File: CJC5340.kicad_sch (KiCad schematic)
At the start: 14 parts

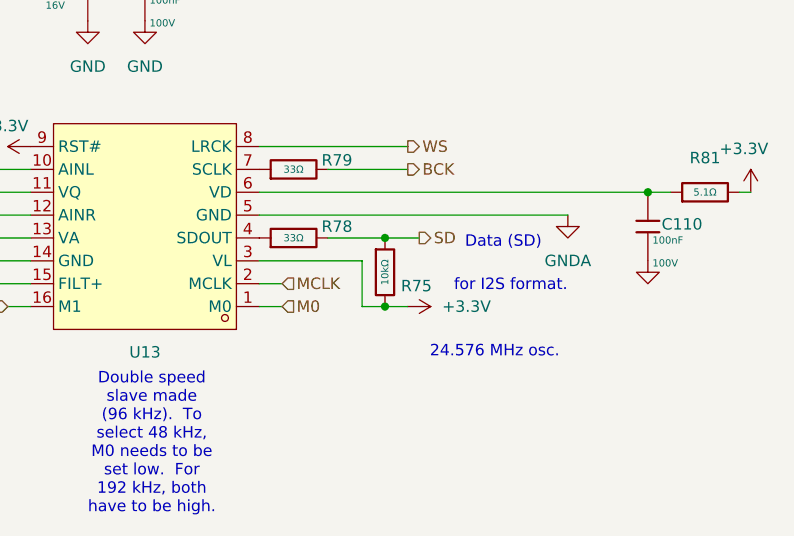
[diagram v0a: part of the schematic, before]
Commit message: Placed the second ADC
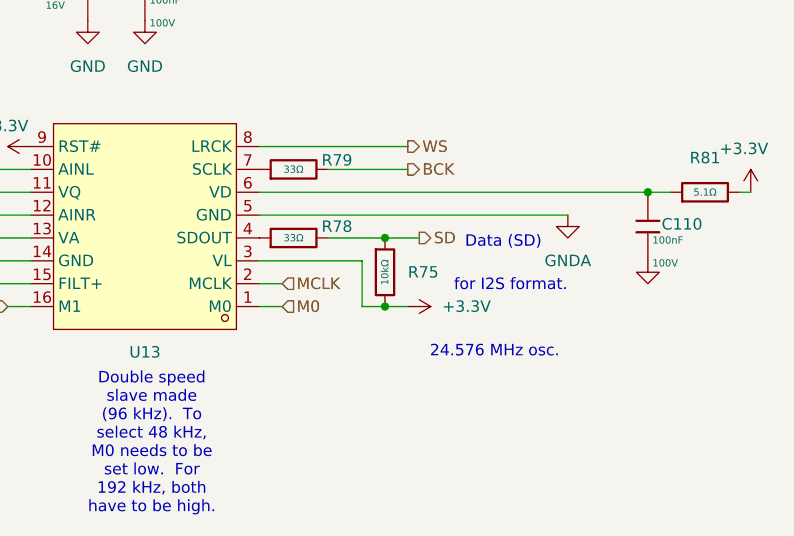
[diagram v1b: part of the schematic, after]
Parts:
- removed R75: 10kΩ, PCM_JLCPCB:R_0402, symbol PCM_JLCPCB-Resistors:0402,10kΩ
- added R75: 10kΩ, PCM_JLCPCB:R_0805, symbol PCM_JLCPCB-Resistors:0805,10kΩ
- C104, C108, C113, C99: Manufacturer AVX -> (none)
- C106, C109, C110, C112, C114: Manufacturer Samsung Electro-Mechanics -> (none)
- R78, R79, R81: Manufacturer UNI-ROYAL(Uniroyal Elec) -> (none)
- U13: Manufacturer ESHINE(光华芯) -> (none)
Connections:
- net +3.3V: now also R75.2
- net SD: now also R75.1

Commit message: More routing
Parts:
- R75: Manufacturer UNI-ROYAL(Uniroyal Elec) -> (none)
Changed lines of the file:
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@@
-			)
-		)
-		(property "Manufacturer" "UNI-ROYAL(Uniroyal Elec)"
-			(at 218.44 93.98 0)
-			(hide yes)
-			(show_name no)
-			(do_not_autoplace no)
-			(effects
-				(font
-					(size 1.27 1.27)
-				)
 			)
 		)

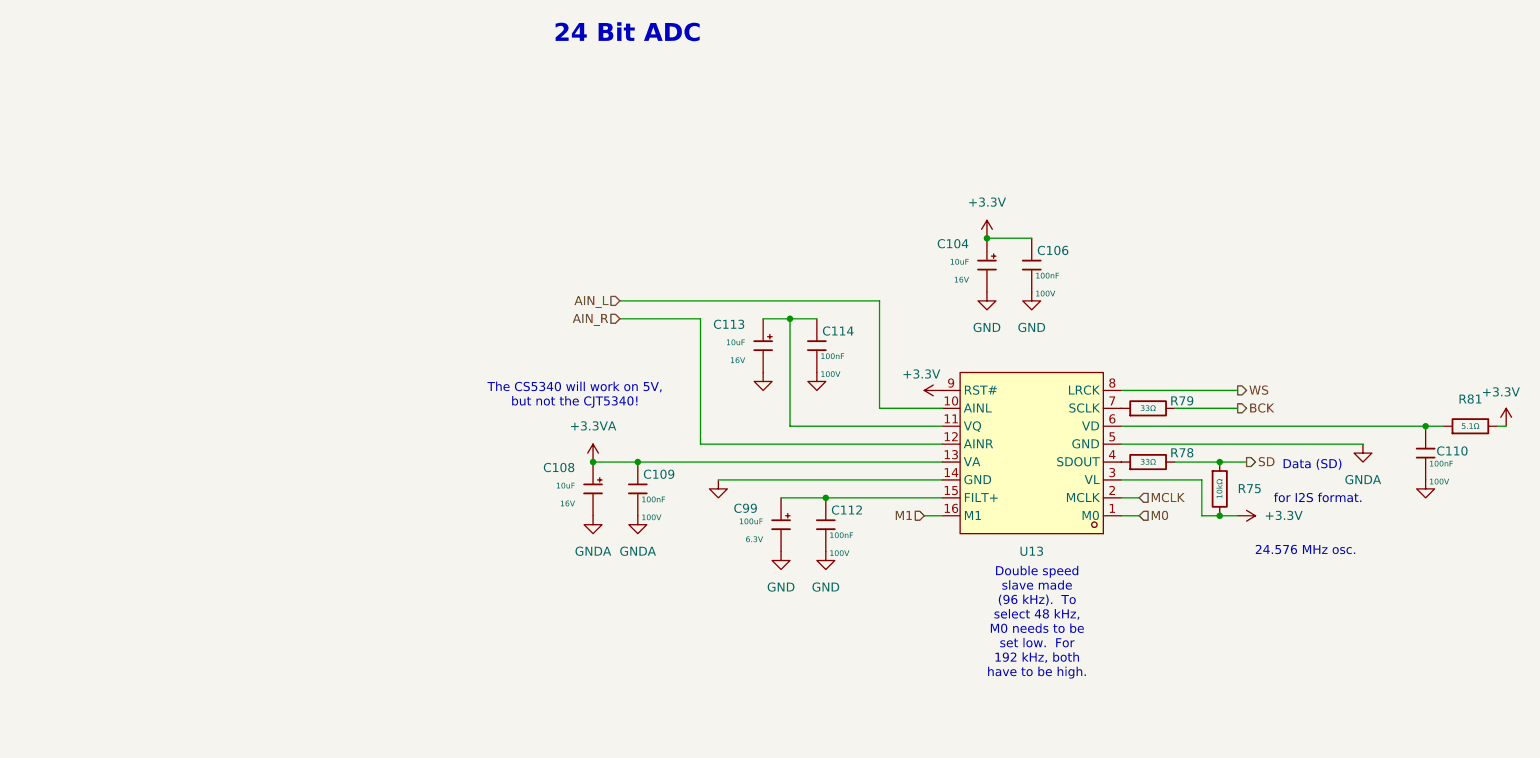
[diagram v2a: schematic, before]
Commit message: Fixed sub-schematic versions
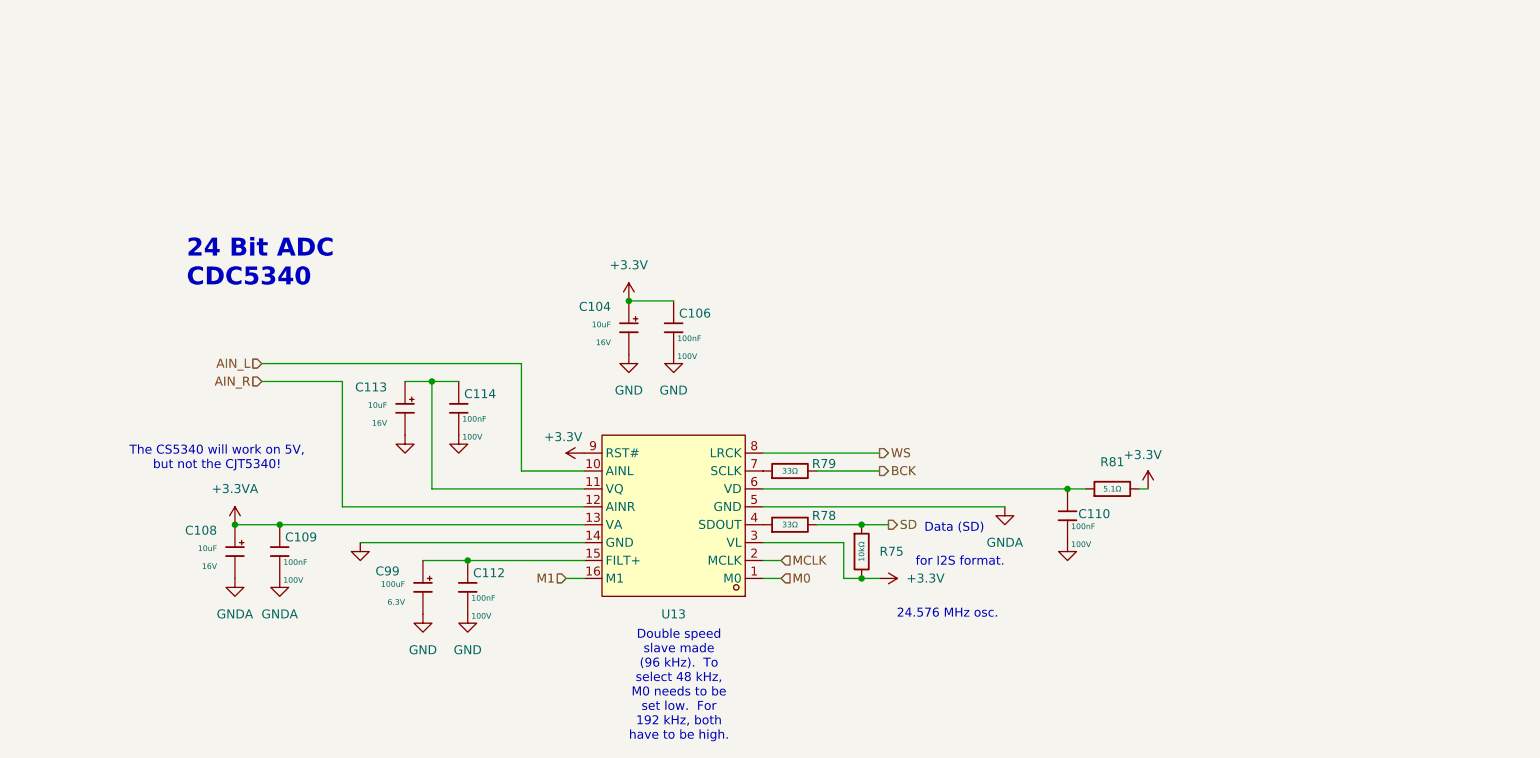
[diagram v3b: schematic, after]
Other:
- note added: "24 Bit ADC CDC5340"
- note removed: "24 Bit ADC"
- moved on the sheet: C104, C106, C108, C109, C110, C112, C113, C114, C99, R75, R78, R79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

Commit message: Changed push pull to PAM8908
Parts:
- U13: LCSC (none) -> C7431487
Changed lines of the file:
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@@
+			)
+		)
+		(property "LCSC" "C7431487"
+			(at 140.97 97.79 0)
+			(hide yes)
+			(show_name no)
+			(do_not_autoplace no)
+			(effects
+				(font
+					(size 1.27 1.27)
+				)
 			)
 		)

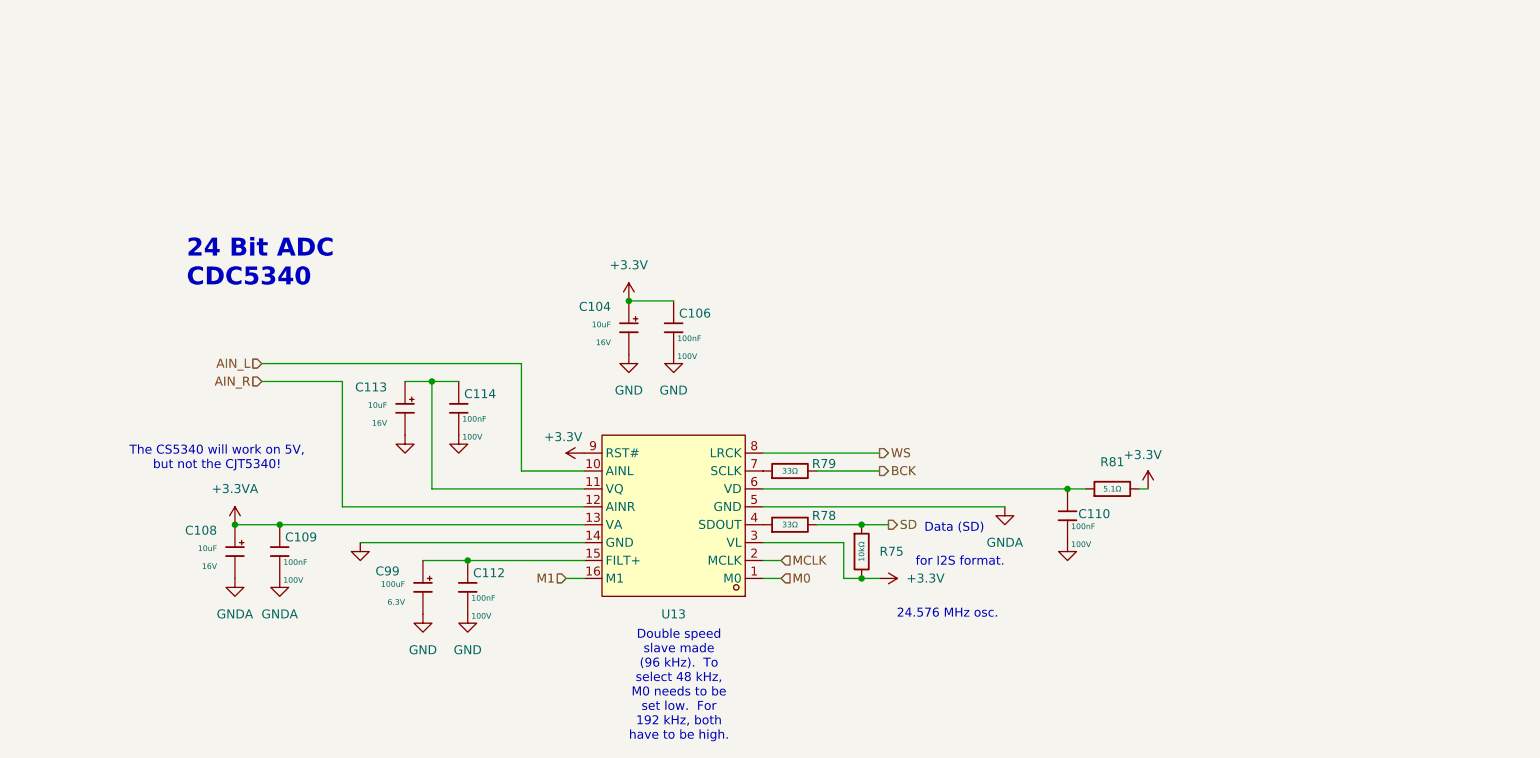
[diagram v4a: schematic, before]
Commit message: Input circuit for the CJT5340
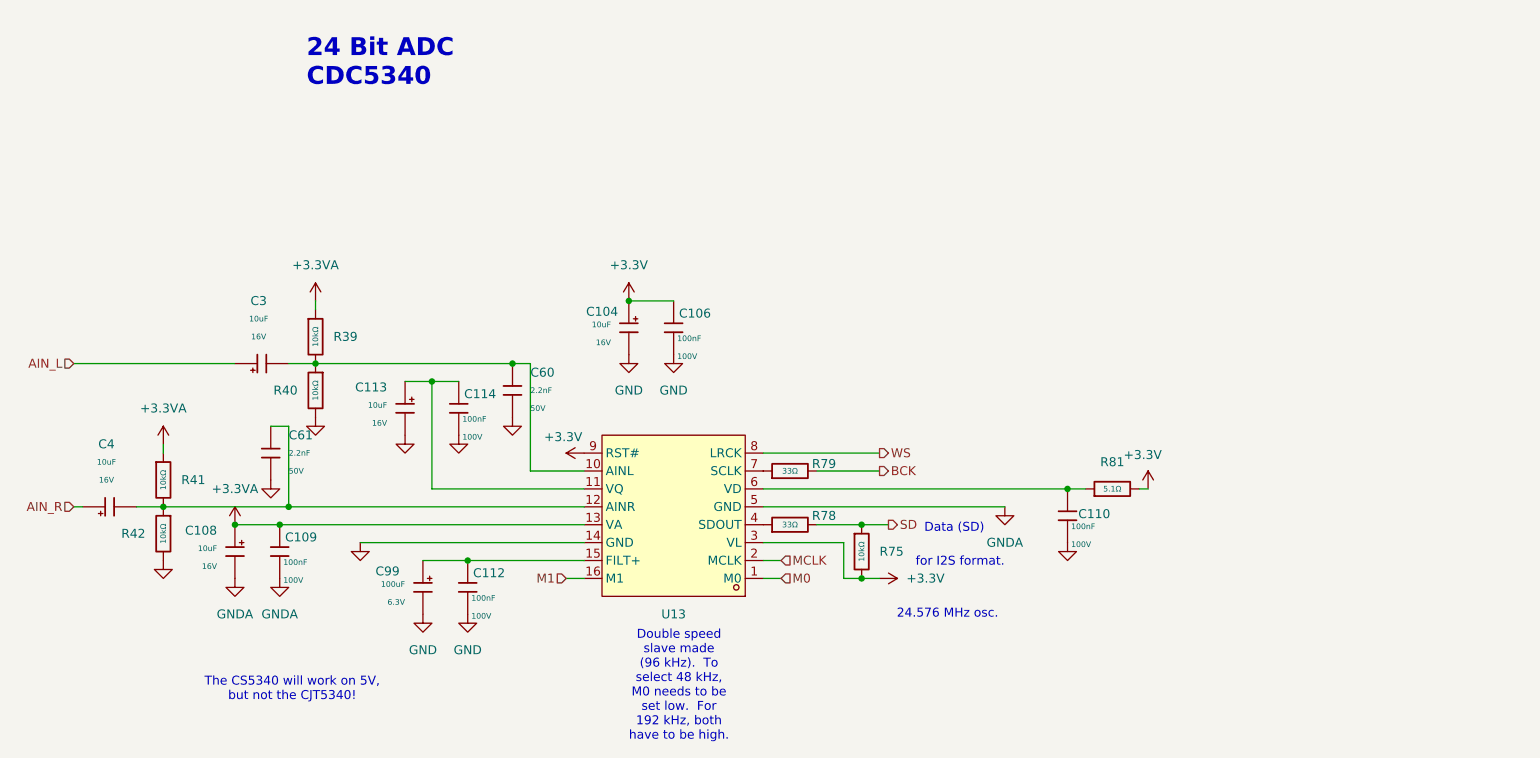
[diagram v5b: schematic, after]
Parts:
- added C3, C4: 10uF, PCM_JLCPCB:C_CASE-A-3216-18(mm), symbol PCM_JLCPCB-Capacitors:CASE-A-3216-18(mm),10uF
- added C60, C61: 2.2nF, PCM_JLCPCB:C_0805, symbol PCM_JLCPCB-Capacitors:0805,2.2nF
- added R39, R40, R41, R42: 10kΩ, PCM_JLCPCB:R_0402, symbol PCM_JLCPCB-Resistors:0402,10kΩ
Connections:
- net +3.3VA: now also R39.1, R41.1
- net AIN_L: now also C3.1; no longer U13.10 (AINL)
- net AIN_R: now also C4.1; no longer U13.12 (AINR)
- net GND: now also C60.2, C61.2, R40.2, R42.2
- new net: C4.2, C61.1, R41.2, R42.1, U13.12 (AINR)
- new net: C3.2, C60.1, R39.2, R40.1, U13.10 (AINL)
